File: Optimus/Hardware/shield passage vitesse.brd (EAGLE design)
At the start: 69.2 x 53.4 mm, 37 parts, among them Q1 2N7000, Q2 2N7000, Q3 2N7000, Q4 2N7000, Q5 2N7000

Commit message: Déplacement des connecteurs à l'intérieur de la carte
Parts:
- moved ALIM_ARDUINO 10.0 mm to (3.17, 14.0), turned to 180 degrees
- moved CONN_MOTOR 9.38 mm to (55.2, 16.9)
- moved R12 7.62 mm to (57.0, 41.3), turned to 0 degrees
- moved BATTERIE 7.62 mm to (13.8, 33.9)
- moved ECU 7.62 mm to (13.8, 39.4)
- moved PALETTE 7.62 mm to (13.8, 46.1)
- moved R11 7.12 mm to (57.0, 38.5), turned to 180 degrees
- moved C4 6.99 mm to (18.5, 49.8)
- moved R13 6.98 mm to (57.3, 35.8)
- moved R14 6.35 mm to (57.3, 32.9)
- moved C5 4.15 mm to (20.7, 34.7), turned to 270 degrees
- moved R15 3.24 mm to (21.1, 46.1)
- moved R17 2.54 mm to (20.6, 42.4)
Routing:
- net IN1_12V: track 3.47 -> 18.3 mm
- net IN0_12V: track 3.41 -> 14.8 mm
- net 12V: track 83.8 -> 94.3 mm
- net OUT4_12V: track 26.2 -> 16.7 mm
- net PALETTE_GAUCHE: track 40.9 -> 31.7 mm
- net SHIFT_CUT: track 46.7 -> 37.5 mm
- net SHIFT_POT: track 50.5 -> 41.3 mm
- net IN0_5V: track 33.3 -> 41.6 mm
- net 5V: track 131.8 -> 124.1 mm
- net IN1_5V: track 27.2 -> 34.2 mm
- net OUT3_12V: track 24.9 -> 18.5 mm
- net N$1: track 8.71 -> 13.9 mm
- net OUT0_12V: track 36.3 -> 31.4 mm
- net OUT2_12V: track 26.7 -> 22.1 mm
- net PALETTE_DROITE: track 47.0 -> 42.7 mm
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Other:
- board text added: "ALIM ARDUINO"

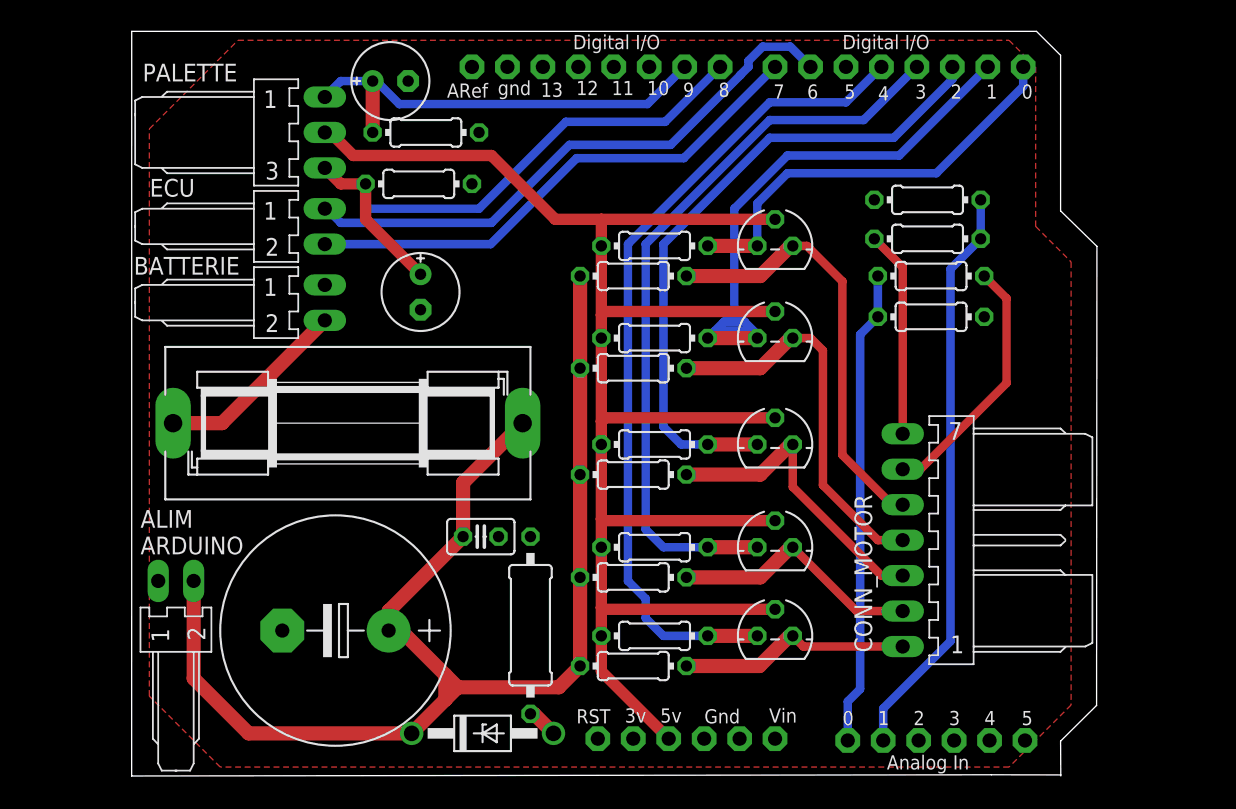
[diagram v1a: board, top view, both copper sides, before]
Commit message: Passage de la Zener à 15V et ajout des convention +5 V et +12V
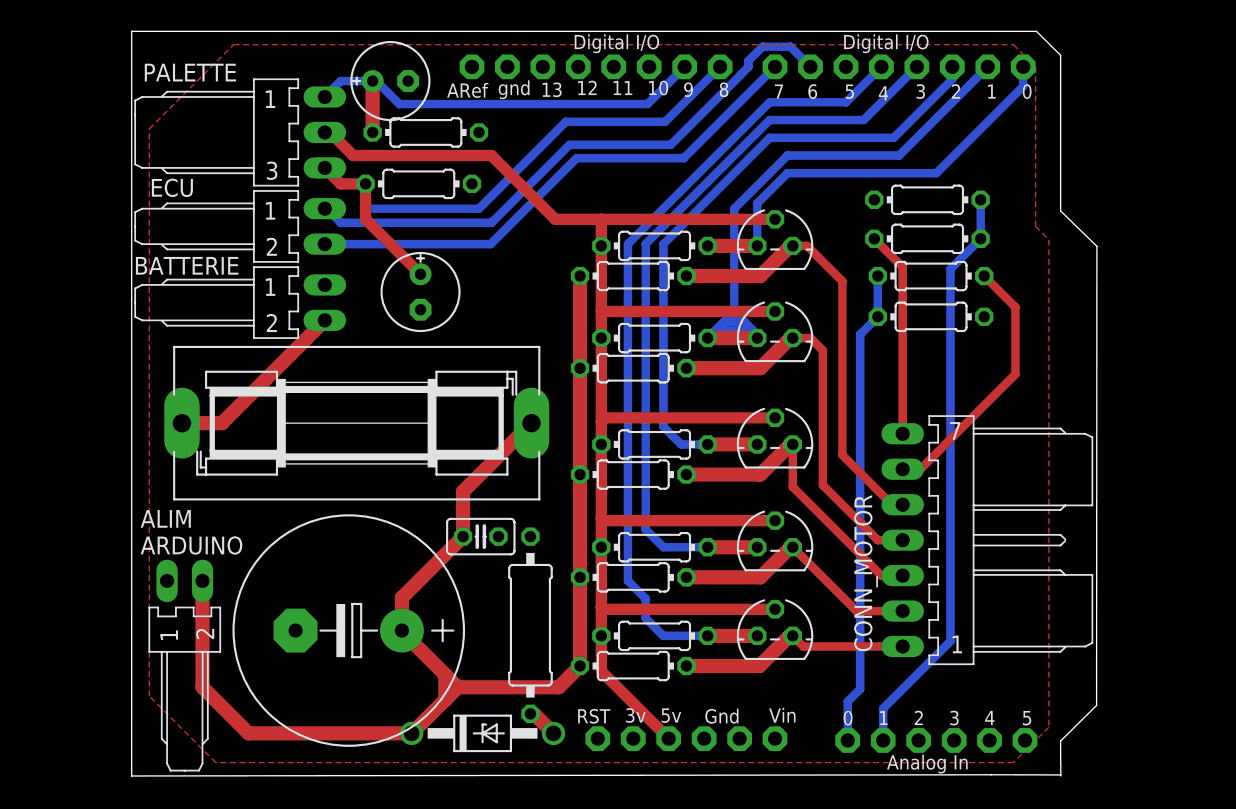
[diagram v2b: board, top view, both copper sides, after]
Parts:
- C4, C5: value 0.33uF -> 0.33µF
- D1: value ZENER 12V -> ZENER 15V
- F1: value 1A -> 2A
- moved C1 0.95 mm to (15.6, 10.4)
- moved F1 0.64 mm to (16.1, 25.3)
- moved ALIM_ARDUINO 0.64 mm to (3.81, 14.0)
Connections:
- net 12V renamed +12V
- net 5V renamed +5V
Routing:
- net +12V: track 94.3 -> 92.4 mm
- net N$1: track 13.9 -> 13.3 mm
- net IN1_12V: track 18.3 -> 18.9 mm
